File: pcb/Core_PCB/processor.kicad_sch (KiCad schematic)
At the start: 6 parts, among them J7 Conn_01x02_MountingPin

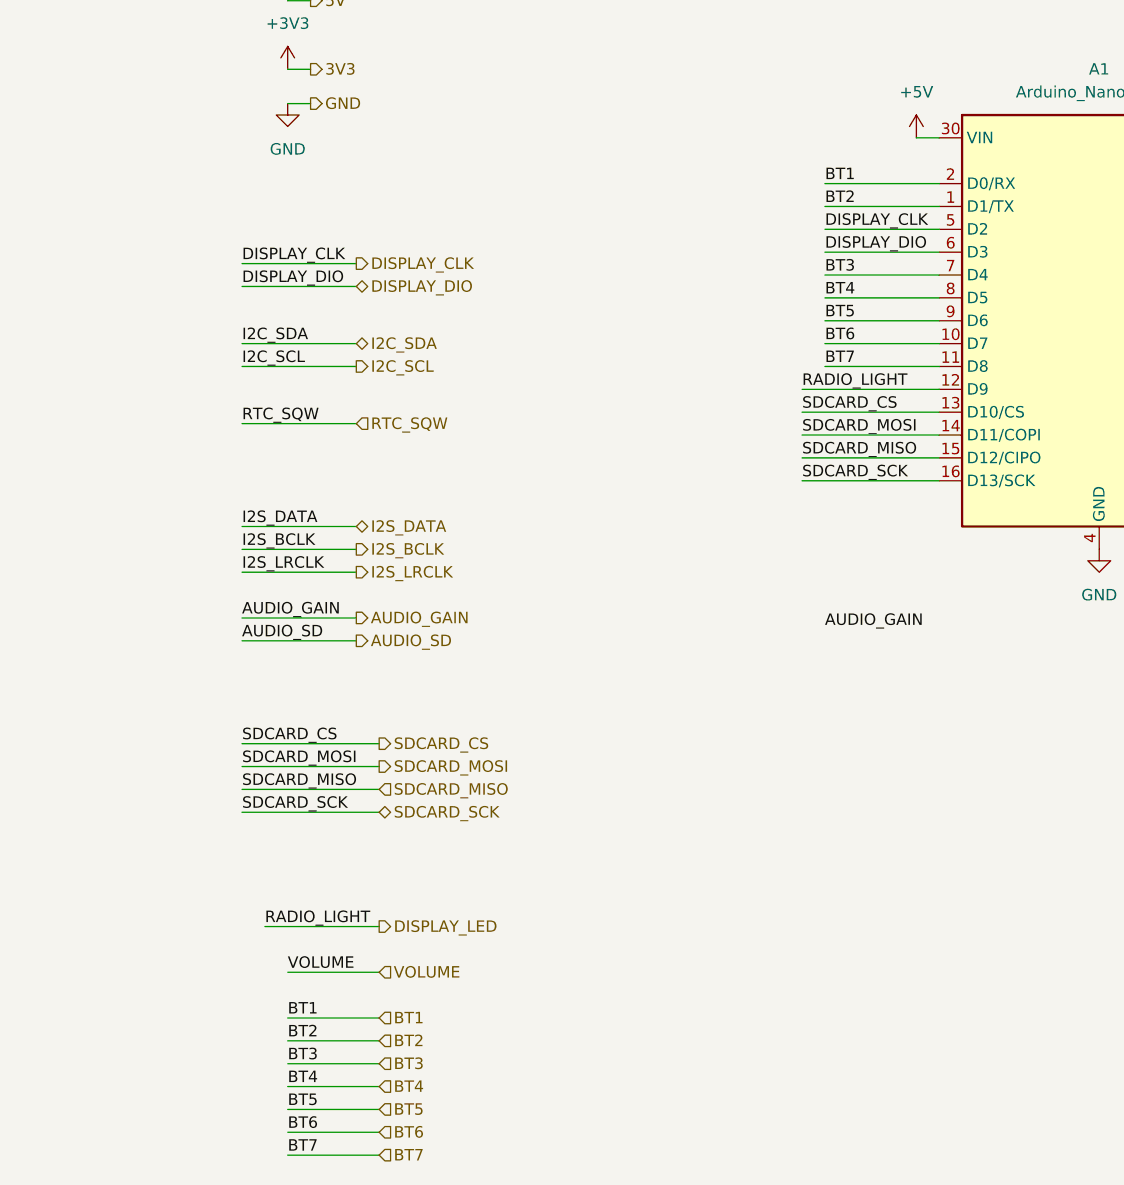
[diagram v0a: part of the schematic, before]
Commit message: SCH: audio gain control via mux (HEF4051), buttons read via i2c io expander (MCP23017)
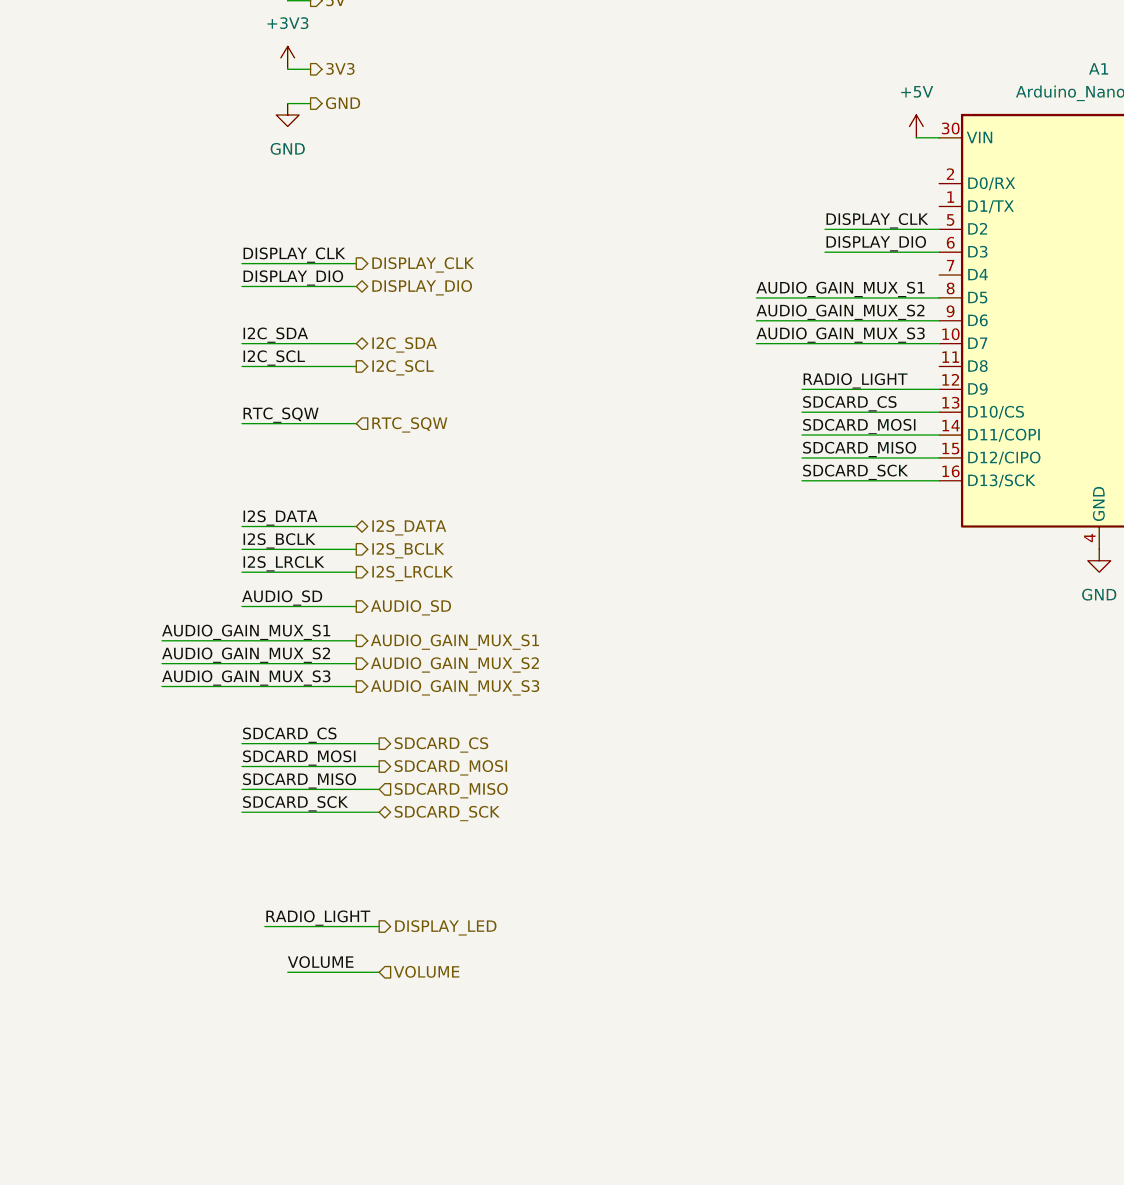
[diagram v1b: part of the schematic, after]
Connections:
- net BT1: no longer names the net of A1.2 (D0/RX)
- net BT2: no longer names the net of A1.1 (D1/TX)
- net BT3: no longer names the net of A1.7 (D4)
- net BT4 renamed AUDIO_GAIN_MUX_S1
- net BT5 renamed AUDIO_GAIN_MUX_S2
- net BT6 renamed AUDIO_GAIN_MUX_S3
- net BT7: no longer names the net of A1.11 (D8)

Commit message: SCH: annotated sheets, reannotated all components
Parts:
- renumbered C12 to C1, C13 to C2, J7 to J1
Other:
- company: (none) -> brunolalb@gmail.com
- title: (none) -> Alarm Clock Resto Mod - Core PCB
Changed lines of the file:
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@@
 	(generator_version "10.0")
 	(paper "A4")
+	(title_block
+		(title "Alarm Clock Resto Mod - Core PCB")
+		(date "2026-07-08")
+		(rev "1.0")
+		(company "brunolalb@gmail.com")
+		(comment 1 "Bruno Landau Albrecht")
+	)
 	(junction
 		(at 160.02 63.5)
@@
 		(dnp no)
 		(fields_autoplaced yes)
-		(property "Reference" "#PWR037"
+		(property "Reference" "#PWR06"
 			(at 49.53 66.04 0)
 			(hide yes)
@@
 			(project "Core_PCB"
 				(path "/79975d02-cfea-4cc3-8869-9743c86248b2/e03c6691-b9bf-461c-8a99-79097618af21"
-					(reference "#PWR037")
+					(reference "#PWR06")
 					(unit 1)
 				)
@@
 		(dnp no)
 		(fields_autoplaced yes)
-		(property "Reference" "#PWR010"
+		(property "Reference" "#PWR09"
 			(at 237.49 76.2 0)
 			(hide yes)
@@
 			(project "Core_PCB"
 				(path "/79975d02-cfea-4cc3-8869-9743c86248b2/e03c6691-b9bf-461c-8a99-79097618af21"
-					(reference "#PWR010")
+					(reference "#PWR09")
 					(unit 1)
 				)
@@
 		(dnp no)
 		(fields_autoplaced yes)
-		(property "Reference" "#PWR040"
+		(property "Reference" "#PWR03"
 			(at 99.06 39.37 0)
 			(hide yes)
@@
 			(project "Core_PCB"
 				(path "/79975d02-cfea-4cc3-8869-9743c86248b2/e03c6691-b9bf-461c-8a99-79097618af21"
-					(reference "#PWR040")
+					(reference "#PWR03")
 					(unit 1)
 				)
@@
 		(dnp no)
 		(fields_autoplaced yes)
-		(property "Reference" "#PWR09"
+		(property "Reference" "#PWR07"
 			(at 119.38 67.31 0)
 			(hide yes)
@@
 			(project "Core_PCB"
 				(path "/79975d02-cfea-4cc3-8869-9743c86248b2/e03c6691-b9bf-461c-8a99-79097618af21"
-					(reference "#PWR09")
+					(reference "#PWR07")
 					(unit 1)
 				)
@@
 		(in_pos_files yes)
 		(dnp no)
-		(property "Reference" "J7"
+		(property "Reference" "J1"
 			(at 85.09 19.05 0)
 			(show_name no)
@@
 			(project "Core_PCB"
 				(path "/79975d02-cfea-4cc3-8869-9743c86248b2/e03c6691-b9bf-461c-8a99-79097618af21"
-					(reference "J7")
+					(reference "J1")
 					(unit 1)
 				)
@@
 		(dnp no)
 		(fields_autoplaced yes)
-		(property "Reference" "#PWR038"
+		(property "Reference" "#PWR05"
 			(at 49.53 59.69 0)
 			(hide yes)
@@
 			(project "Core_PCB"
 				(path "/79975d02-cfea-4cc3-8869-9743c86248b2/e03c6691-b9bf-461c-8a99-79097618af21"
-					(reference "#PWR038")
+					(reference "#PWR05")
 					(unit 1)
 				)
@@
 		(dnp no)
 		(fields_autoplaced yes)
-		(property "Reference" "C13"
+		(property "Reference" "C2"
 			(at 114.3 27.9399 0)
 			(show_name no)
@@
 			(project "Core_PCB"
 				(path "/79975d02-cfea-4cc3-8869-9743c86248b2/e03c6691-b9bf-461c-8a99-79097618af21"
-					(reference "C13")
+					(reference "C2")
 					(unit 1)
 				)
@@
 		(dnp no)
 		(fields_autoplaced yes)
-		(property "Reference" "C12"
+		(property "Reference" "C1"
 			(at 102.87 27.0509 0)
 			(show_name no)
@@
 			(project "Core_PCB"
 				(path "/79975d02-cfea-4cc3-8869-9743c86248b2/e03c6691-b9bf-461c-8a99-79097618af21"
-					(reference "C12")
+					(reference "C1")
 					(unit 1)
 				)
@@
 		(dnp no)
 		(fields_autoplaced yes)
-		(property "Reference" "#PWR039"
+		(property "Reference" "#PWR01"
 			(at 99.06 29.21 0)
 			(hide yes)
@@
 			(project "Core_PCB"
 				(path "/79975d02-cfea-4cc3-8869-9743c86248b2/e03c6691-b9bf-461c-8a99-79097618af21"
-					(reference "#PWR039")
+					(reference "#PWR01")
 					(unit 1)
 				)
@@
 		(dnp no)
 		(fields_autoplaced yes)
-		(property "Reference" "#PWR05"
+		(property "Reference" "#PWR08"
 			(at 160.02 67.31 0)
 			(hide yes)
@@
 			(project "Core_PCB"
 				(path "/79975d02-cfea-4cc3-8869-9743c86248b2/e03c6691-b9bf-461c-8a99-79097618af21"
-					(reference "#PWR05")
+					(reference "#PWR08")
 					(unit 1)
 				)
@@
 		(dnp no)
 		(fields_autoplaced yes)
-		(property "Reference" "#PWR036"
+		(property "Reference" "#PWR04"
 			(at 49.53 52.07 0)
 			(hide yes)
@@
 			(project "Core_PCB"
 				(path "/79975d02-cfea-4cc3-8869-9743c86248b2/e03c6691-b9bf-461c-8a99-79097618af21"
-					(reference "#PWR036")
+					(reference "#PWR04")
 					(unit 1)
 				)
@@
 		(dnp no)
 		(fields_autoplaced yes)
-		(property "Reference" "#PWR08"
+		(property "Reference" "#PWR011"
 			(at 139.7 115.57 0)
 			(hide yes)
@@
 			(project "Core_PCB"
 				(path "/79975d02-cfea-4cc3-8869-9743c86248b2/e03c6691-b9bf-461c-8a99-79097618af21"
-					(reference "#PWR08")
+					(reference "#PWR011")
 					(unit 1)
 				)
@@
 		(dnp no)
 		(fields_autoplaced yes)
-		(property "Reference" "#PWR041"
+		(property "Reference" "#PWR02"
 			(at 85.09 39.37 0)
 			(hide yes)
@@
 			(project "Core_PCB"
 				(path "/79975d02-cfea-4cc3-8869-9743c86248b2/e03c6691-b9bf-461c-8a99-79097618af21"
-					(reference "#PWR041")
+					(reference "#PWR02")
 					(unit 1)
 				)
@@
 		(dnp no)
 		(fields_autoplaced yes)
-		(property "Reference" "#PWR035"
+		(property "Reference" "#PWR010"
 			(at 237.49 88.9 0)
 			(hide yes)
@@
 			(project "Core_PCB"
 				(path "/79975d02-cfea-4cc3-8869-9743c86248b2/e03c6691-b9bf-461c-8a99-79097618af21"
-					(reference "#PWR035")
+					(reference "#PWR010")
 					(unit 1)
 				)

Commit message: SCH: assigned footprints to what had missing, replaced some polarized caps with non polarized, added connector for capacitance sensor, ran electric test and fixed minor issues
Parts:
- BOOT0, BOOT1: footprint (none) -> Button_Switch_THT:SW_PUSH_6mm
- C1: footprint (none) -> Capacitor_THT:CP_Radial_D4.0mm_P2.00mm
- C2: footprint (none) -> Capacitor_SMD:C_0603_1608Metric_Pad1.08x0.95mm_HandSolder
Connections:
- net DISPLAY_LED renamed RADIO_LIGHT
- no-connect marks 0 -> 6
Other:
- moved on the sheet: C1, C2

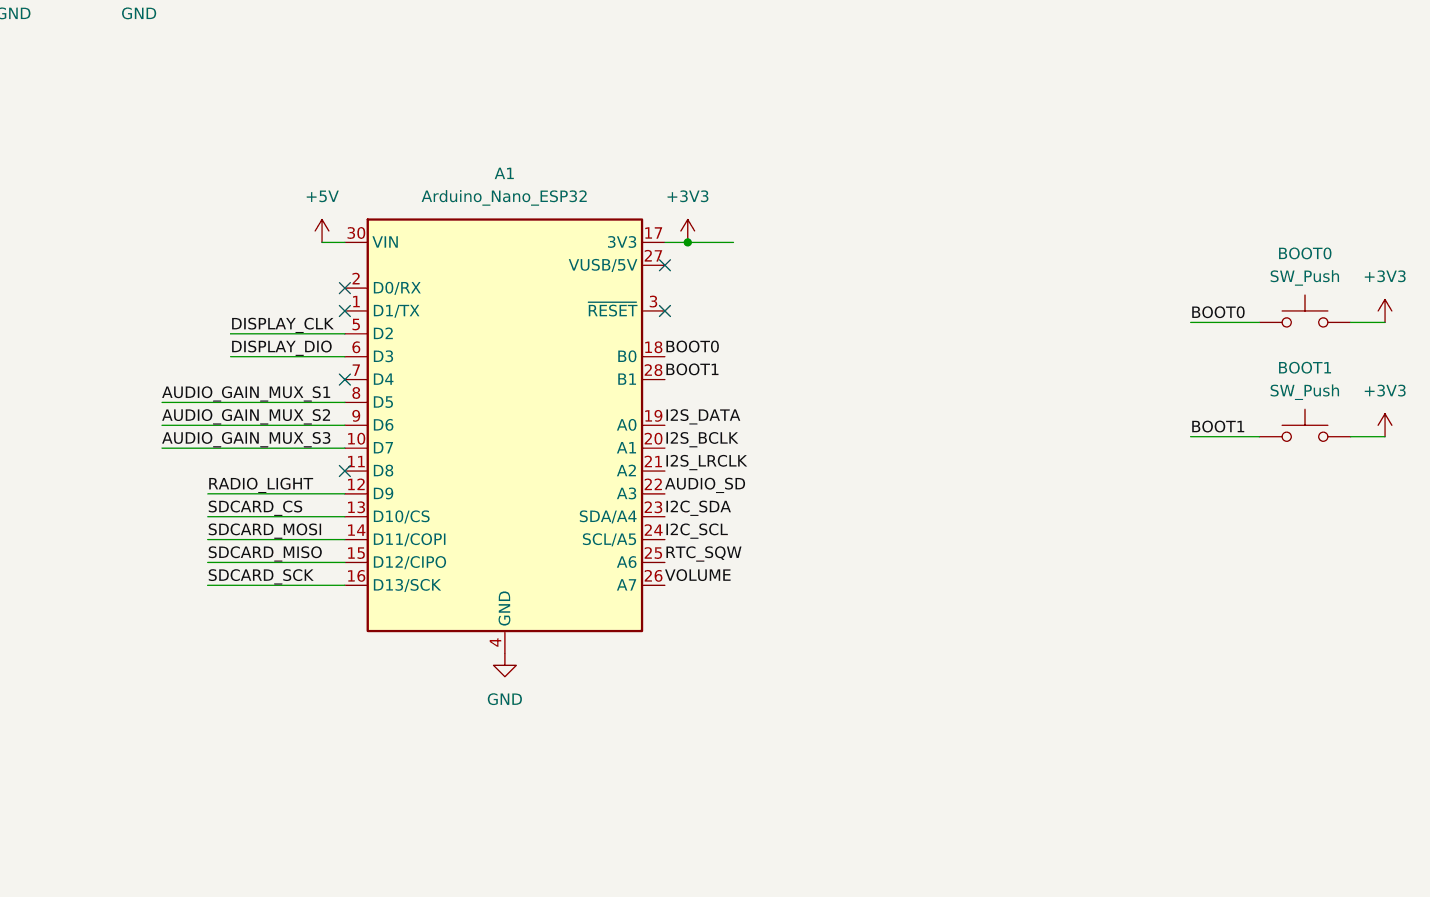
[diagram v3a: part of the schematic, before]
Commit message: SCH - audio: screw terminal was facing the wrong direction; buttons: volume pot had wrong footprint, added +5V input; processor: use alternative arduino symbol and custom footprint (with 3d model), added reset switch, adjusted rule for PWR lines
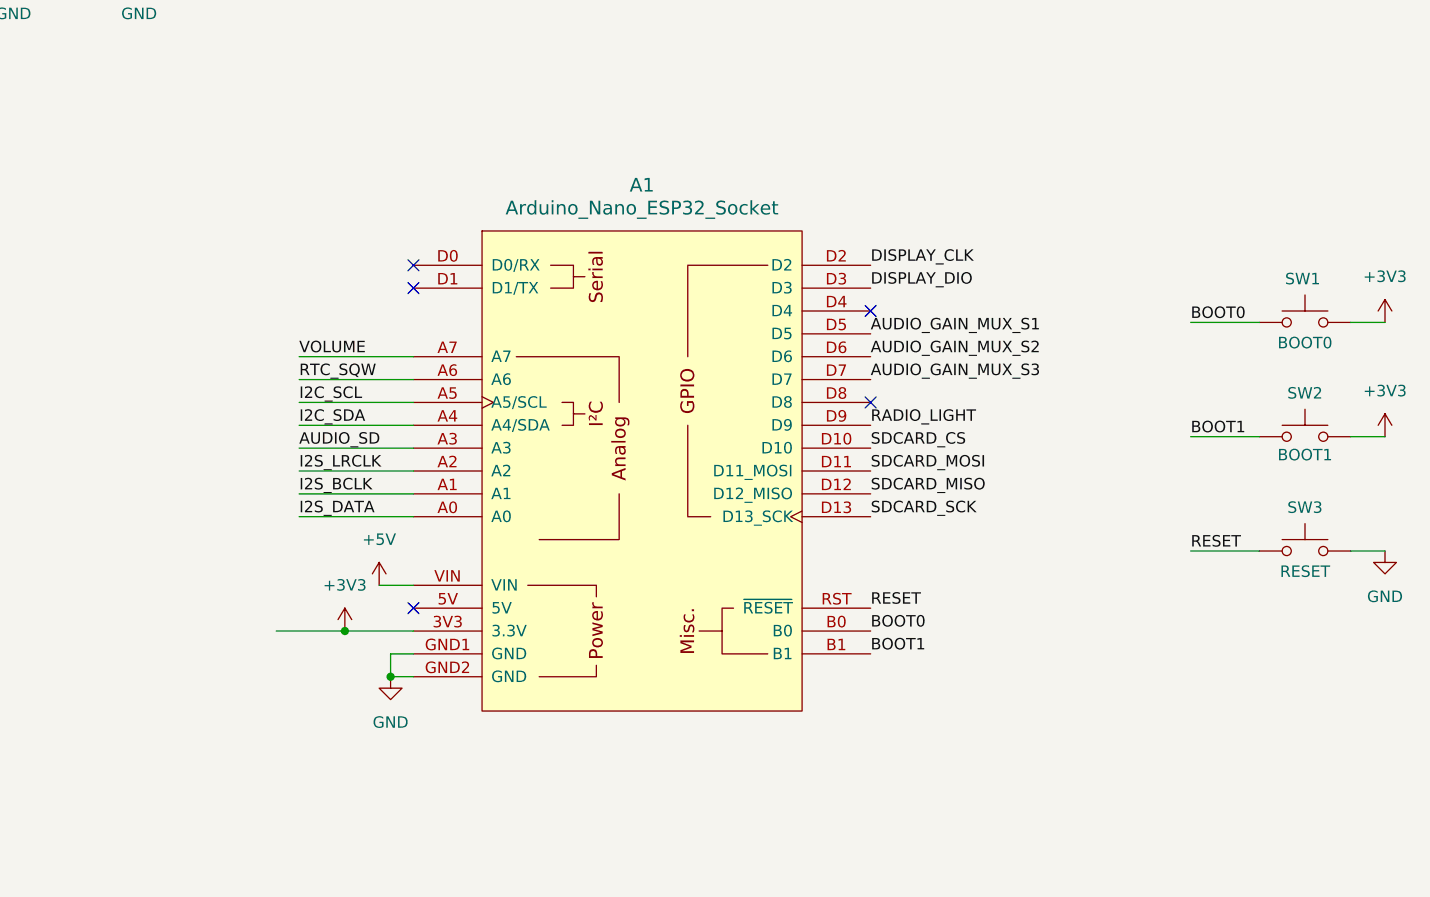
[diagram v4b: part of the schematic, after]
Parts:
- removed A1: Arduino_Nano_ESP32, Module:Arduino_Nano, symbol MCU_Module:Arduino_Nano_ESP32
- added A1: Arduino_Nano_ESP32_Socket, RadioWecker:Arduino_Nano_ESP32_Socket, symbol PCM_arduino-library:Arduino_Nano_ESP32_Socket
- added SW3: SW_Push, Button_Switch_THT:SW_PUSH_6mm, symbol Switch:SW_Push
- SW1: renamed from BOOT0; Name (none) -> BOOT0
- SW2: renamed from BOOT1; Name (none) -> BOOT1
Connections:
- net +3V3: now also A1.3V3 (3.3V)
- net +5V: now also A1.VIN
- net AUDIO_GAIN_MUX_S1: now also A1.D5
- net AUDIO_GAIN_MUX_S2: now also A1.D6
- net AUDIO_GAIN_MUX_S3: now also A1.D7
- net AUDIO_SD: now also A1.A3
- net BOOT0: now also A1.B0
- net BOOT1: now also A1.B1
- net DISPLAY_CLK: now also A1.D2
- net DISPLAY_DIO: now also A1.D3
- net GND: now also A1.GND1 (GND), A1.GND2 (GND), SW3.2
- net I2C_SCL: now also A1.A5 (A5/SCL)
- net I2C_SDA: now also A1.A4 (A4/SDA)
- net I2S_BCLK: now also A1.A1
- net I2S_DATA: now also A1.A0
- net I2S_LRCLK: now also A1.A2
- net RADIO_LIGHT: now also A1.D9
- net RTC_SQW: now also A1.A6
- net SDCARD_CS: now also A1.D10
- net SDCARD_MISO: now also A1.D12 (D12_MISO)
- net SDCARD_MOSI: now also A1.D11 (D11_MOSI)
- net SDCARD_SCK: now also A1.D13 (D13_SCK)
- net VOLUME: now also A1.A7
- new net RESET: A1.RST (~{RESET}), SW3.1
- no-connect marks 6 -> 5

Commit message: PCB - initial layout
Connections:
- net DISPLAY_CLK: now also A1.D4; no longer A1.D2
- net RTC_SQW: now also A1.D2; no longer A1.A6

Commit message: PCBs: updated logo; added I2C resistors to I2C (core pcb)
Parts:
- added R20, R21: 2K2, Resistor_SMD:R_0603_1608Metric_Pad0.98x0.95mm_HandSolder, symbol Device:R
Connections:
- net +3V3: now also R20.1, R21.1
- net I2C_SCL: now also R21.2
- net I2C_SDA: now also R20.2
